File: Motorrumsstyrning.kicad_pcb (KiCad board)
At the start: 2 copper layers, 56 x 48 mm, 4 parts

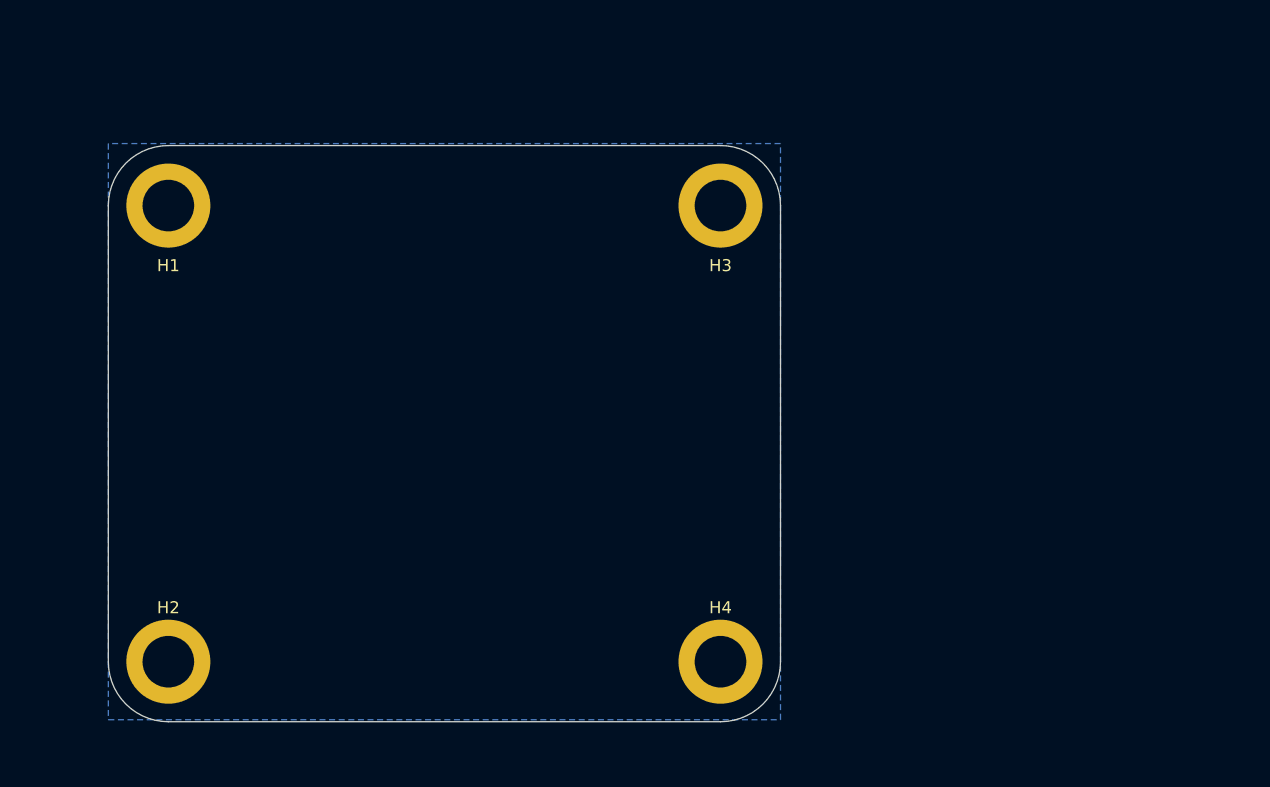
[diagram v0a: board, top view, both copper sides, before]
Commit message: Added symbols, worked on schematic and PCB
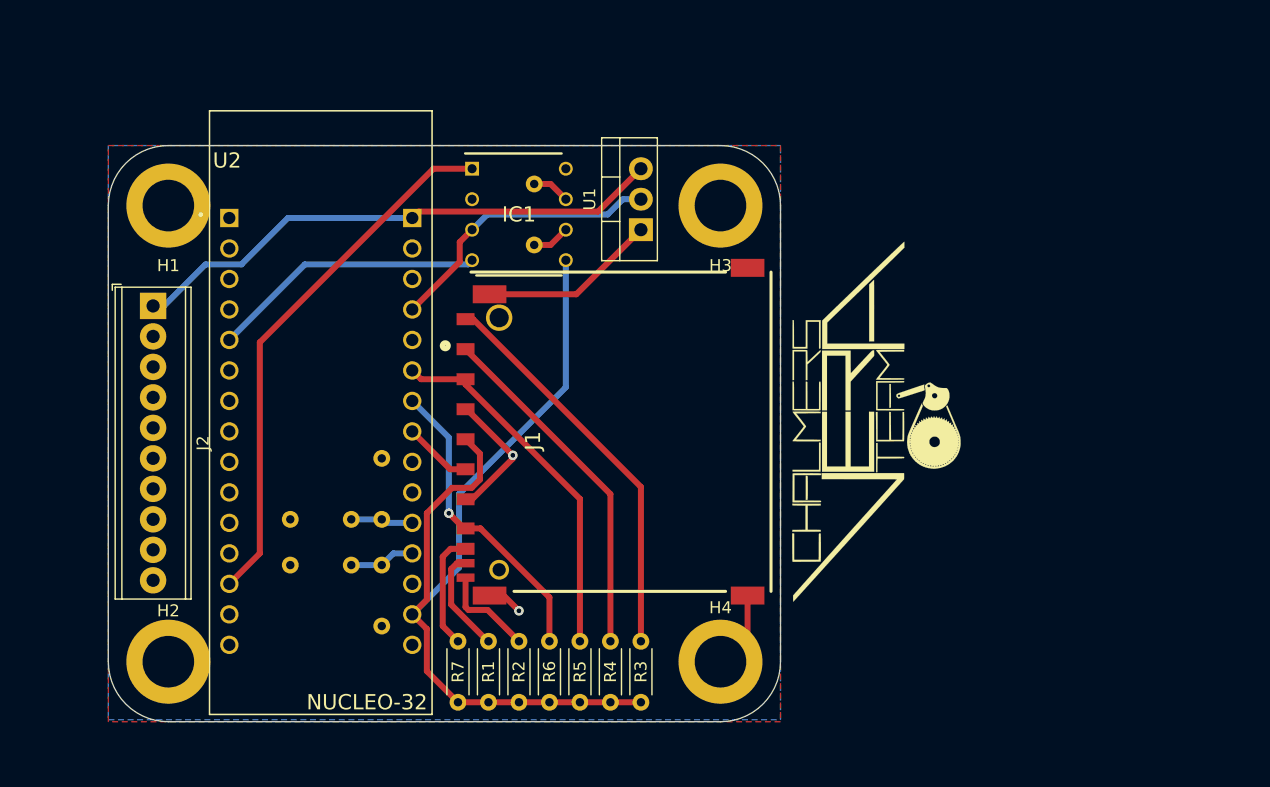
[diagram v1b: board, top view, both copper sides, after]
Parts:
- added G***: LOGO, Vera-MRS-21:Vera-Logo, F.Cu at (186.0, 96.0)
- added IC1: MCP2562-E_P, Vera-MRS-21:DIP781W56P254L950H533Q8N, F.Cu at (156.2, 78.7)
- added J1: SD_Card_Connector, Vera-MRS-21:2041021-3_2, F.Cu at (152.2, 110.1)
- added J2: Screw_Terminal_01x14, TerminalBlock_Phoenix:TerminalBlock_Phoenix_MPT-0,5-10-2.54_1x10_P2.54mm_Horizontal, F.Cu at (125.7, 86.4)
- added R1: 50k, Resistor_THT:R_Axial_DIN0204_L3.6mm_D1.6mm_P5.08mm_Horizontal, F.Cu at (153.7, 119.4)
- added R10: 4k2, Resistor_THT:R_Axial_DIN0204_L3.6mm_D1.6mm_P5.08mm_Horizontal, B.Cu at (137.2, 108.0)
- added R11: 10k, Resistor_THT:R_Axial_DIN0204_L3.6mm_D1.6mm_P5.08mm_Horizontal, B.Cu at (144.8, 108.0)
- added R12: 120R, Resistor_THT:R_Axial_DIN0204_L3.6mm_D1.6mm_P5.08mm_Horizontal, B.Cu at (157.5, 76.2)
- added R2: 50k, Resistor_THT:R_Axial_DIN0204_L3.6mm_D1.6mm_P5.08mm_Horizontal, F.Cu at (156.2, 119.4)
- added R3: 50k, Resistor_THT:R_Axial_DIN0204_L3.6mm_D1.6mm_P5.08mm_Horizontal, F.Cu at (166.4, 119.4)
- added R4: 50k, Resistor_THT:R_Axial_DIN0204_L3.6mm_D1.6mm_P5.08mm_Horizontal, F.Cu at (163.8, 119.4)
- added R5: 50k, Resistor_THT:R_Axial_DIN0204_L3.6mm_D1.6mm_P5.08mm_Horizontal, F.Cu at (161.3, 119.4)
- added R6: 50k, Resistor_THT:R_Axial_DIN0204_L3.6mm_D1.6mm_P5.08mm_Horizontal, F.Cu at (158.8, 119.4)
- added R7: 50k, Resistor_THT:R_Axial_DIN0204_L3.6mm_D1.6mm_P5.08mm_Horizontal, F.Cu at (151.1, 119.4)
- added R8: 4k2, Resistor_THT:R_Axial_DIN0204_L3.6mm_D1.6mm_P5.08mm_Horizontal, B.Cu at (137.2, 104.1)
- added R9: 10k, Resistor_THT:R_Axial_DIN0204_L3.6mm_D1.6mm_P5.08mm_Horizontal, B.Cu at (144.8, 104.1)
- added U1: LM1084-5.0, Package_TO_SOT_THT:TO-220-3_Vertical, F.Cu at (166.4, 80.0)
- added U2: NUCLEO-F303K8, Vera-MRS-21:NUCLEO_32, F.Cu at (139.7, 95.2)
- H1, H2, H3, H4: value MountingHole_Pad -> M4_Hole
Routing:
- net +3V3: track 0.00 -> 77.3 mm
- net +12V: track 0.00 -> 45.4 mm
- net /CAN_RX: track 0.00 -> 44.8 mm
- net GND: track 0.00 -> 35.7 mm, vias 0 -> 2
- net Net-(J1-Pad9): track 0.00 -> 33.3 mm
- net /SPI1_MOSI: track 0.00 -> 30.5 mm
- net /~SPI1_CS: track 0.00 -> 29.3 mm
- net /SPI1_MISO: track 0.00 -> 25.6 mm, vias 0 -> 1
- net +5V: track 0.00 -> 23.8 mm
- net /CAN_TX: track 0.00 -> 23.0 mm
- net Net-(J1-Pad8): track 0.00 -> 9.75 mm
- net /~CD: track 0.00 -> 8.74 mm
- net /~WP: track 0.00 -> 8.09 mm
- net /SPI1_SCK: track 0.00 -> 5.74 mm
- net /Deadmans: track 0.00 -> 5.48 mm
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- added copper zone on F.Cu, net GND
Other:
- rule trace_min: 0.2 -> 0.1
- rule via_min_drill: 0.3 -> 0.21
- rule via_min_size: 0.4 -> 0.45

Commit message: Large PCB first design
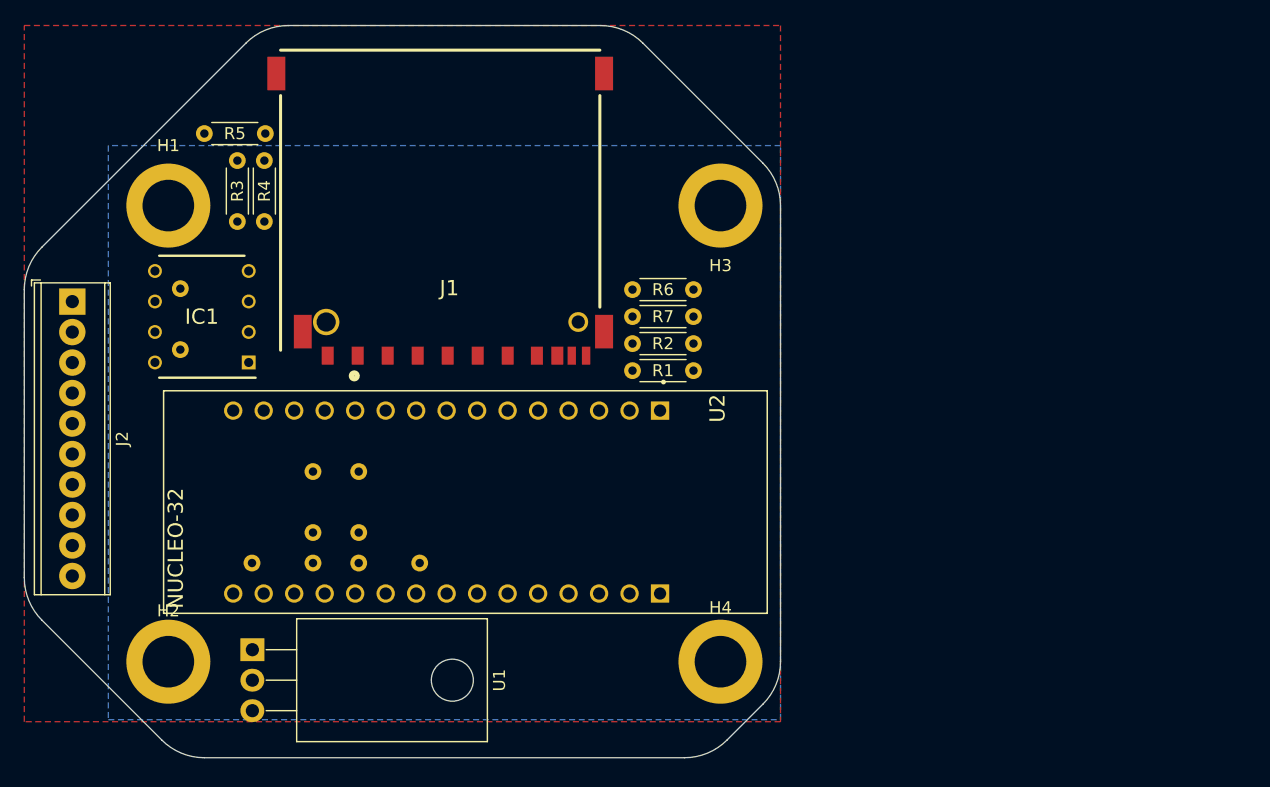
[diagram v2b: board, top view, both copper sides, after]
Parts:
- removed G***: LOGO, Vera-MRS-21:Vera-Logo
- U1: footprint Package_TO_SOT_THT:TO-220-3_Vertical -> Package_TO_SOT_THT:TO-220-3_Horizontal_TabDown
- moved R5 56.8 mm to (130.0, 72.0), turned to 0 degrees
- moved R3 56.3 mm to (132.8, 74.2), turned to 270 degrees
- moved R4 53.6 mm to (135.0, 74.2), turned to 270 degrees
- moved U1 47.7 mm to (134.0, 115.0), turned to 270 degrees
- moved R7 37.6 mm to (170.8, 87.2), turned to 180 degrees
- moved R6 36.4 mm to (170.8, 85.0), turned to 180 degrees
- moved R2 33.2 mm to (170.8, 89.5), turned to 180 degrees
- moved R12 32.6 mm to (128.0, 90.0), turned to 90 degrees
- moved R1 32.5 mm to (170.8, 91.8), turned to 180 degrees
- moved IC1 27.8 mm to (129.8, 87.3), turned to 180 degrees
- moved J1 22.8 mm to (162.9, 90.0), turned to 180 degrees
- moved U2 14.2 mm to (151.8, 102.7), turned to 270 degrees
- moved R10 8.02 mm to (139.1, 100.2), turned to 270 degrees
- moved R8 6.95 mm to (142.9, 100.2), turned to 270 degrees
- moved J2 6.74 mm to (119.0, 86.0)
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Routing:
- net +3V3: track 77.3 -> 0.00 mm
- net +12V: track 45.4 -> 0.00 mm
- net /CAN_RX: track 44.8 -> 0.00 mm
- net GND: track 35.7 -> 0.00 mm, vias 2 -> 0
- net Net-(J1-Pad9): track 33.3 -> 0.00 mm
- net /SPI1_MOSI: track 30.5 -> 0.00 mm
- net /~SPI1_CS: track 29.3 -> 0.00 mm
- net /SPI1_MISO: track 25.6 -> 0.00 mm, vias 1 -> 0
- net +5V: track 23.8 -> 0.00 mm
- net /CAN_TX: track 23.0 -> 0.00 mm
- net Net-(J1-Pad8): track 9.75 -> 0.00 mm
- net /~CD: track 8.74 -> 0.00 mm
- net /~WP: track 8.09 -> 0.00 mm
- net /SPI1_SCK: track 5.74 -> 0.00 mm
- net /Deadmans: track 5.48 -> 0.00 mm
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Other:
- board size 56 x 48 mm -> 63 x 61 mm

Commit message: Added small logo, moved parts
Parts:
- added G***: LOGO, Vera-MRS-21:Vera-Logo-Small, F.Cu at (162.0, 118.0)
- moved R5 28.3 mm to (150.1, 91.9), turned to 180 degrees
- moved R6 19.9 mm to (152.1, 91.9), turned to 0 degrees
- moved R4 17.9 mm to (137.9, 91.9), turned to 0 degrees
- moved R3 17.9 mm to (135.4, 91.9), turned to 90 degrees
- moved R7 7.95 mm to (164.3, 91.9)
- moved J1 2.07 mm to (163.2, 88.0)
- moved R2 1.31 mm to (171.4, 88.4)
- moved R1 1.28 mm to (171.4, 90.7)
- moved R12 1.27 mm to (126.7, 90.0)
- moved IC1 1.27 mm to (128.5, 87.3)

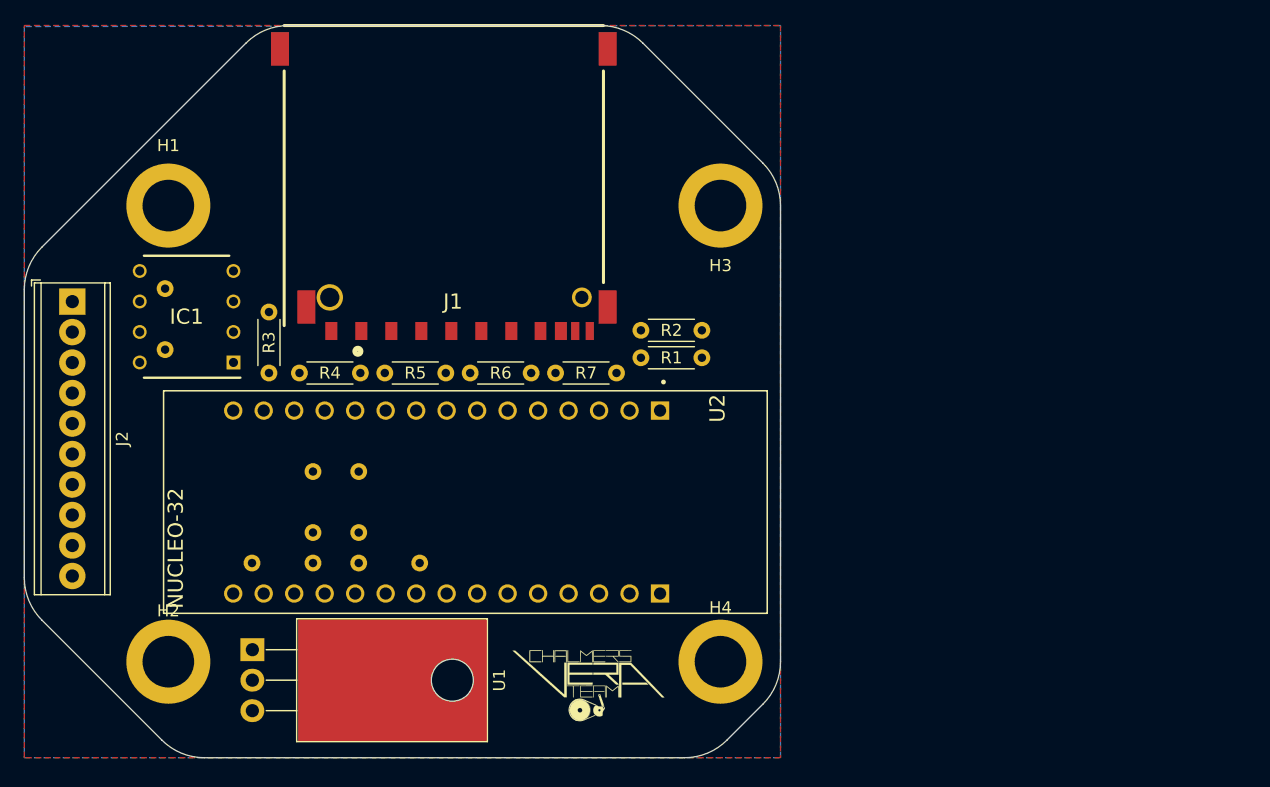
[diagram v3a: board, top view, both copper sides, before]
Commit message: Added Testpoints, Ziptie slots, I2C pull-ups
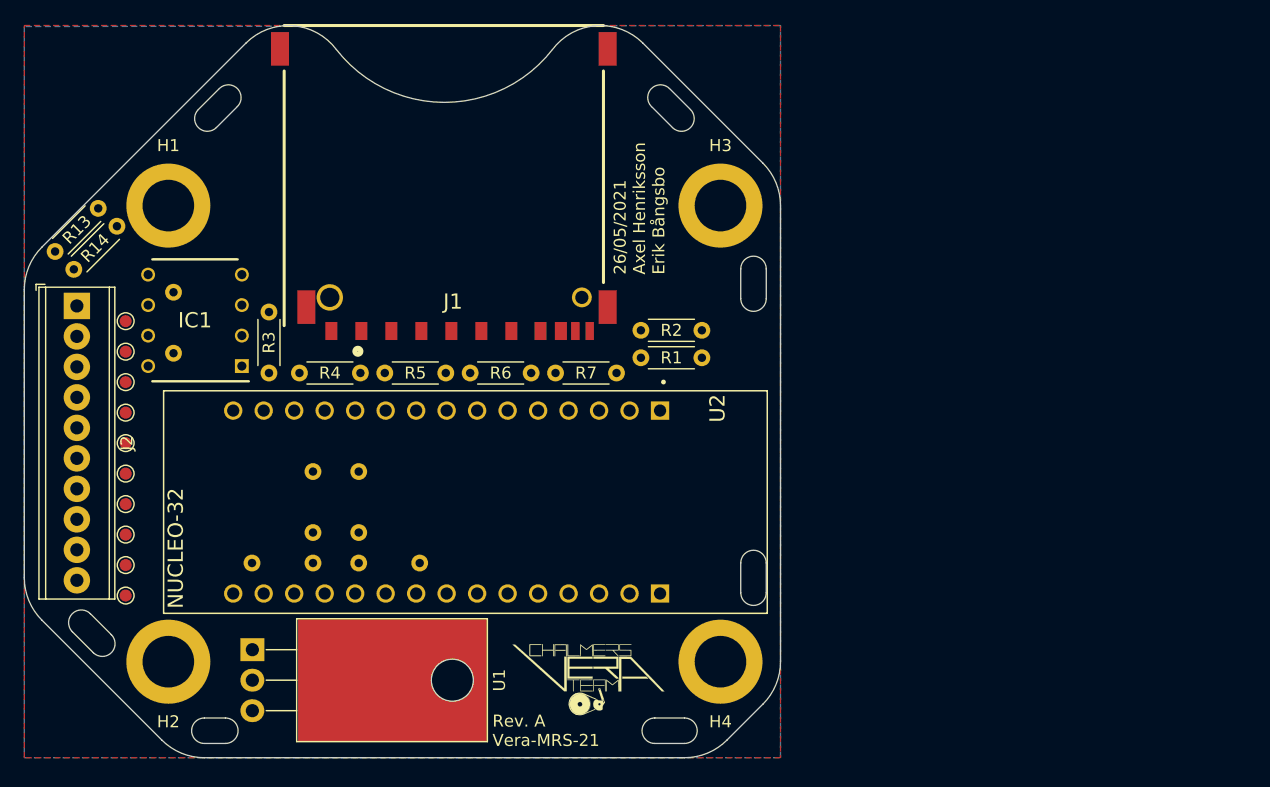
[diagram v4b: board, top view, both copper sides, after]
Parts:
- added R13: 1k, Resistor_THT:R_Axial_DIN0204_L3.6mm_D1.6mm_P5.08mm_Horizontal, F.Cu at (121.2, 78.2)
- added R14: 1k, Resistor_THT:R_Axial_DIN0204_L3.6mm_D1.6mm_P5.08mm_Horizontal, F.Cu at (122.7, 79.7)
- added TP1: TestPoint_Small, TestPoint:TestPoint_Pad_D1.0mm, F.Cu at (123.4, 87.6)
- added TP10: TestPoint_Small, TestPoint:TestPoint_Pad_D1.0mm, F.Cu at (123.4, 100.3)
- added TP11: TestPoint_Small, TestPoint:TestPoint_Pad_D1.0mm, F.Cu at (123.4, 102.9)
- added TP12: TestPoint_Small, TestPoint:TestPoint_Pad_D1.0mm, F.Cu at (123.4, 105.4)
- added TP13: TestPoint_Small, TestPoint:TestPoint_Pad_D1.0mm, F.Cu at (123.4, 108.0)
- added TP14: TestPoint_Small, TestPoint:TestPoint_Pad_D1.0mm, F.Cu at (123.4, 110.5)
- added TP6: TestPoint_Small, TestPoint:TestPoint_Pad_D1.0mm, F.Cu at (123.4, 90.2)
- added TP7: TestPoint_Small, TestPoint:TestPoint_Pad_D1.0mm, F.Cu at (123.4, 92.7)
- added TP8: TestPoint_Small, TestPoint:TestPoint_Pad_D1.0mm, F.Cu at (123.4, 95.2)
- added TP9: TestPoint_Small, TestPoint:TestPoint_Pad_D1.0mm, F.Cu at (123.4, 97.8)
- J2: value Screw_Terminal_01x14 -> Screw_Terminal_01x10
- moved R12 0.76 mm to (127.4, 90.3)
- moved IC1 0.76 mm to (129.2, 87.6)
- moved J2 0.52 mm to (119.4, 86.4)
- moved G*** 0.50 mm to (162.0, 117.5)
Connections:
- J2 pad 10: Net-(J2-Pad10) -> GND
- J2 pad 2: Net-(J2-Pad2) -> /I2C1_SDA
- J2 pad 3: Net-(J2-Pad3) -> /I2C1_SCL
- J2 pad 4: Net-(J2-Pad4) -> /CANH
- J2 pad 5: Net-(J2-Pad5) -> /CANL
- J2 pad 7: Net-(J2-Pad7) -> /Start_Relay_GND
- J2 pad 8: Net-(J2-Pad8) -> /Tach_12V
- J2 pad 9: Net-(J2-Pad9) -> /Deadmans_12V
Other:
- outline, holes or cut-outs redrawn
- board text added: "26/05/2021 Axel Henriksson Erik Bångsbo"
- board text added: "Rev. A Vera-MRS-21"

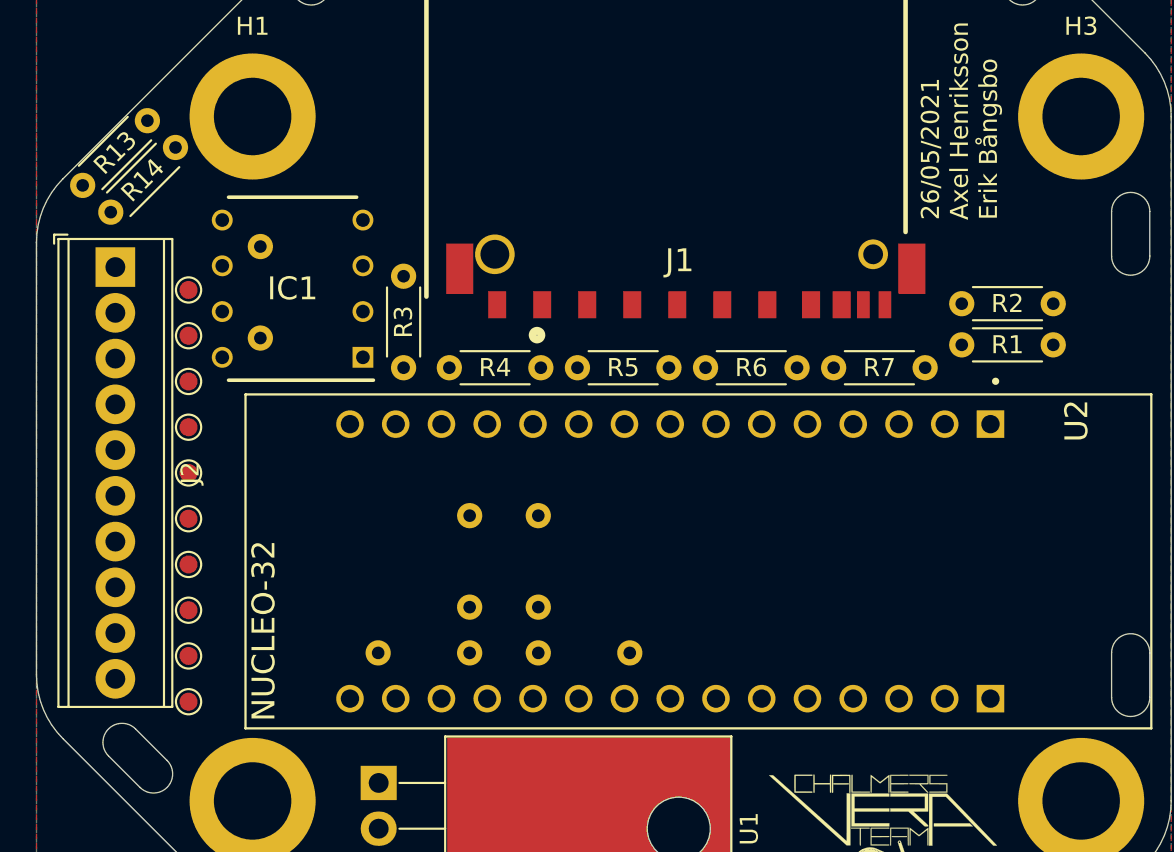
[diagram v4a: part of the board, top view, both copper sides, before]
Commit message: Moved terminal block, Added Testpoint labels
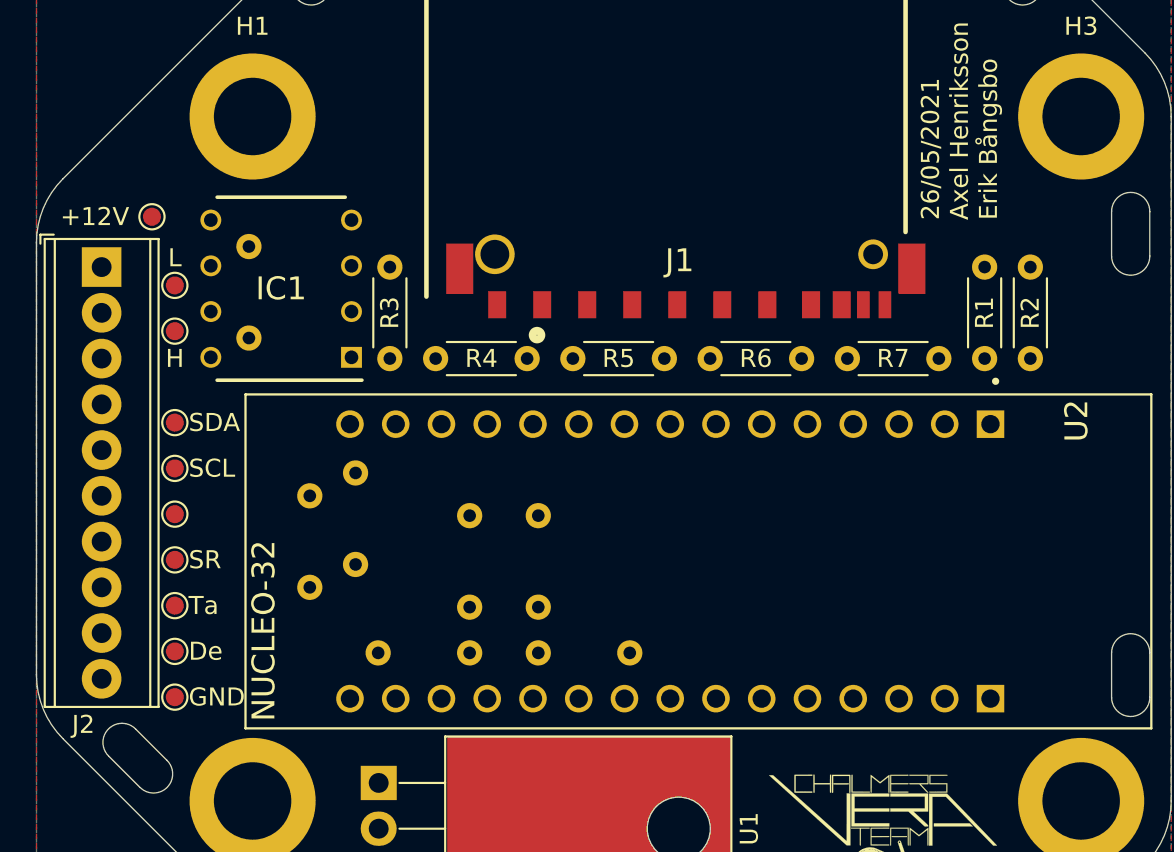
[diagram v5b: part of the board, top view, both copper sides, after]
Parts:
- R13, R14: moved to B.Cu
- moved R13 27.4 mm to (130.2, 104.1), turned to 90 degrees
- moved R14 25.2 mm to (132.7, 102.9), turned to 90 degrees
- moved R1 5.76 mm to (167.6, 86.4), turned to 270 degrees
- moved R3 5.64 mm to (134.6, 86.4), turned to 270 degrees
- moved TP1 4.54 mm to (121.4, 83.6)
- moved TP6 2.90 mm to (122.7, 87.4)
- moved TP7 2.90 mm to (122.7, 89.9)
- moved R2 2.40 mm to (170.2, 86.4), turned to 270 degrees
- moved R4 0.92 mm to (137.2, 91.4)
- moved R7 0.92 mm to (165.1, 91.4)
- moved TP10 0.80 mm to (122.7, 100.1)
- moved TP11 0.80 mm to (122.7, 102.6)
- moved TP13 0.80 mm to (122.7, 107.7)
- moved TP8 0.80 mm to (122.7, 95.0)
- moved TP9 0.80 mm to (122.7, 97.5)
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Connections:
- J2 pad 2: /I2C1_SDA -> /CANL
- J2 pad 3: /I2C1_SCL -> /CANH
- J2 pad 4: /CANH -> /I2C1_SDA
- J2 pad 5: /CANL -> /I2C1_SCL
- TP6 pad 1: /I2C1_SDA -> /CANL
- TP7 pad 1: /I2C1_SCL -> /CANH
- TP8 pad 1: /CANH -> /I2C1_SDA
- TP9 pad 1: /CANL -> /I2C1_SCL
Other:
- board text added: "+12V"
- board text added: "De"
- board text added: "GND"
- board text added: "H"
- board text added: "L"
- board text added: "SCL"
- board text added: "SDA"
- board text added: "SR"
- board text added: "Ta"
